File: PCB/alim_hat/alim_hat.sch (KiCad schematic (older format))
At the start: 42 parts, among them J1 Screw_Terminal_01x04, J10 Conn_01x02, J11 Conn_01x02, J12 Conn_01x02, J2 XT30, J3 Conn_02x04_Odd_Even, J4 Jack-DC, J5 Jack-DC, J6 Jack-DC, J7 Jack-DC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

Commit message: complet new polarity protection
update fab file
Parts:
- added D1: MM1Z15, Diode_SMD:D_SOD-123, symbol Device:D_Zener
- added R14: 470k, Resistor_SMD:R_0805_2012Metric, symbol Device:R
- R13: LCSC (none) -> C17513
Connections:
- net GND: now also D1.2 (A), R14.2
- net at Q1.1 (G), R13.2: now also D1.1 (K), R14.1
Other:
- moved on the sheet: Q1, R13
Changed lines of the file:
@@
 L Transistor_FET:IRF540N Q1
 U 1 1 5F94BD9C
-P 7350 2650
-F 0 "Q1" V 7599 2650 50  0000 C CNN
-F 1 "IRFS7530TRLPBF" V 7690 2650 50  0000 C CNN
-F 2 "Package_TO_SOT_SMD:TO-263-2" H 7600 2575 50  0001 L CIN
-F 3 "http://www.irf.com/product-info/datasheets/data/irf540n.pdf" H 7350 2650 50  0001 L CNN
-F 4 "C500544" V 7350 2650 50  0001 C CNN "LCSC"
-	1    7350 2650
-	0    1    1    0
+P 7300 2750
+F 0 "Q1" V 7549 2750 50  0000 C CNN
+F 1 "IRFS7530TRLPBF" V 7640 2750 50  0000 C CNN
+F 2 "Package_TO_SOT_SMD:TO-263-2" H 7550 2675 50  0001 L CIN
+F 3 "http://www.irf.com/product-info/datasheets/data/irf540n.pdf" H 7300 2750 50  0001 L CNN
+F 4 "C500544" V 7300 2750 50  0001 C CNN "LCSC"
+	1    7300 2750
+	0    -1   1    0
 $EndComp
 $Comp
@@
 L power:+12V #PWR0101
 U 1 1 5F9723E9
-P 7350 2150
-F 0 "#PWR0101" H 7350 2000 50  0001 C CNN
-F 1 "+12V" V 7365 2278 50  0000 L CNN
-F 2 "" H 7350 2150 50  0001 C CNN
-F 3 "" H 7350 2150 50  0001 C CNN
-	1    7350 2150
+P 7300 2250
+F 0 "#PWR0101" H 7300 2100 50  0001 C CNN
+F 1 "+12V" V 7315 2378 50  0000 L CNN
+F 2 "" H 7300 2250 50  0001 C CNN
+F 3 "" H 7300 2250 50  0001 C CNN
+	1    7300 2250
 	1    0    0    -1
 $EndComp
@@
 L Device:R R13
 U 1 1 5F972BB9
-P 7350 2300
-F 0 "R13" H 7420 2346 50  0000 L CNN
-F 1 "1k" V 7350 2250 50  0000 L CNN
-F 2 "Resistor_SMD:R_0805_2012Metric" V 7280 2300 50  0001 C CNN
-F 3 "~" H 7350 2300 50  0001 C CNN
-	1    7350 2300
+P 7300 2400
+F 0 "R13" H 7370 2446 50  0000 L CNN
+F 1 "1k" V 7300 2350 50  0000 L CNN
+F 2 "Resistor_SMD:R_0805_2012Metric" V 7230 2400 50  0001 C CNN
+F 3 "~" H 7300 2400 50  0001 C CNN
+F 4 "C17513" H 7300 2400 50  0001 C CNN "LCSC"
+	1    7300 2400
 	1    0    0    -1
 $EndComp
@@
 	-1   0    0    1
 $EndComp
-Text Label 7550 2750 0    50   ~ 0
+Text Label 7100 2850 2    50   ~ 0
 gnd_no
 $Comp
 L power:GND #PWR0105
 U 1 1 5F9B3CAE
-P 7150 2750
-F 0 "#PWR0105" H 7150 2500 50  0001 C CNN
-F 1 "GND" V 7155 2622 50  0000 R CNN
-F 2 "" H 7150 2750 50  0001 C CNN
-F 3 "" H 7150 2750 50  0001 C CNN
-	1    7150 2750
-	0    1    1    0
+P 7850 2850
+F 0 "#PWR0105" H 7850 2600 50  0001 C CNN
+F 1 "GND" V 7855 2722 50  0000 R CNN
+F 2 "" H 7850 2850 50  0001 C CNN
+F 3 "" H 7850 2850 50  0001 C CNN
+	1    7850 2850
+	0    -1   -1   0
 $EndComp
 Text Label 9400 4250 2    50   ~ 0
 gnd_no
 Wire Notes Line
-	6650 1600 8100 1600
-Wire Notes Line
-	8100 1600 8100 3250
-Wire Notes Line
-	8100 3250 6650 3250
+	8300 1600 8300 3250
 Wire Notes Line
 	6650 3250 6650 1600
@@
 	-1   0    0    -1
 $EndComp
+$Comp
+L Device:R R14
+U 1 1 5F99B8E4
+P 7600 2700
+F 0 "R14" H 7670 2746 50  0000 L CNN
+F 1 "470k" V 7600 2600 50  0000 L CNN
+F 2 "Resistor_SMD:R_0805_2012Metric" V 7530 2700 50  0001 C CNN
+F 3 "~" H 7600 2700 50  0001 C CNN
+F 4 "C17709" H 7600 2700 50  0001 C CNN "LCSC"
+	1    7600 2700
+	1    0    0    -1
+$EndComp
+$Comp
+L Device:D_Zener D1
+U 1 1 5F9A9262
+P 7850 2700
+F 0 "D1" V 7804 2779 50  0000 L CNN
+F 1 "MM1Z15" V 7895 2779 50  0000 L CNN
+F 2 "Diode_SMD:D_SOD-123" H 7850 2700 50  0001 C CNN
+F 3 "~" H 7850 2700 50  0001 C CNN
+F 4 "C86235" V 7850 2700 50  0001 C CNN "LCSC"
+	1    7850 2700
+	0    1    1    0
+$EndComp
+Wire Wire Line
+	7500 2850 7600 2850
+Connection ~ 7600 2850
+Wire Wire Line
+	7600 2850 7850 2850
+Connection ~ 7850 2850
+Wire Wire Line
+	7850 2550 7600 2550
+Connection ~ 7600 2550
+Wire Wire Line
+	7300 2550 7600 2550
+Connection ~ 7300 2550
+Wire Notes Line
+	6650 1600 8300 1600
+Wire Notes Line
+	6650 3250 8300 3250
 $EndSCHEMATC

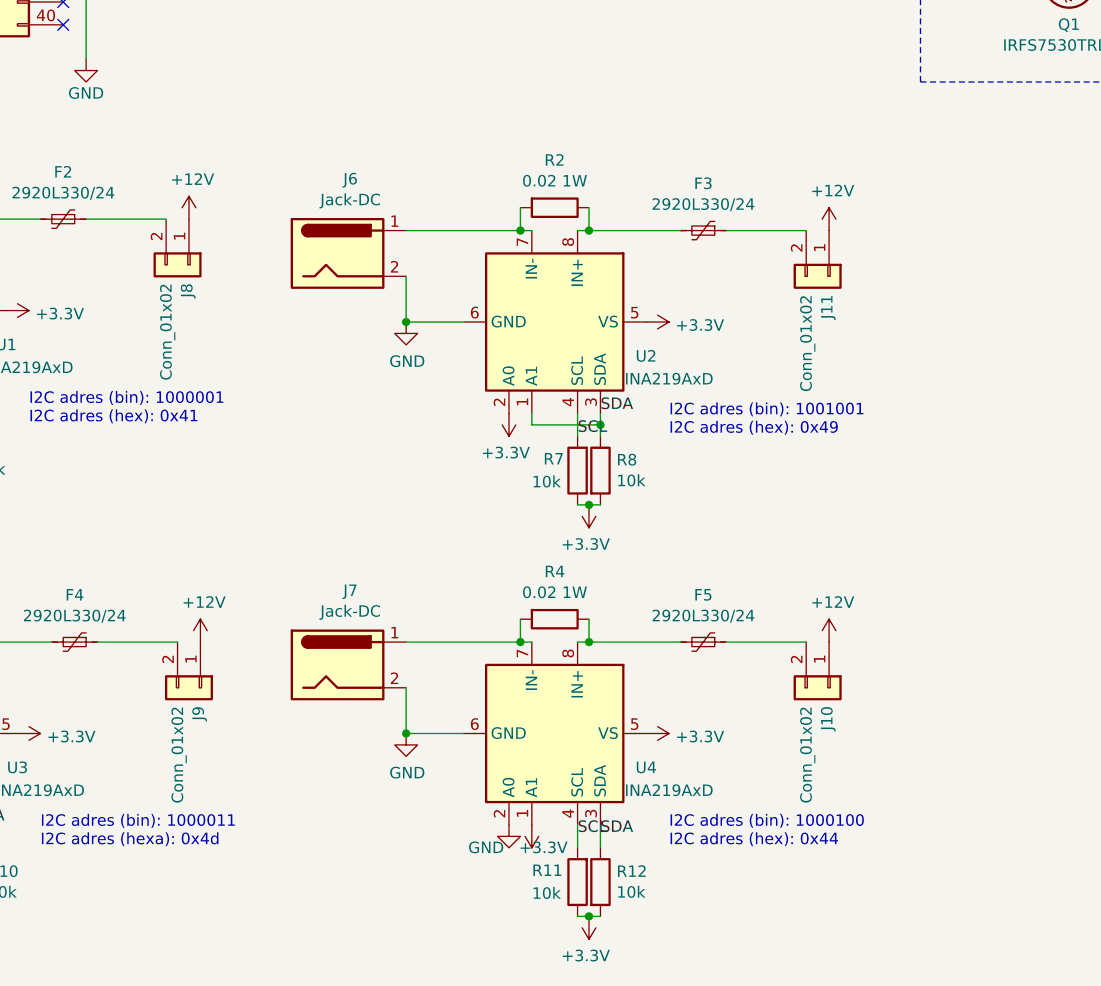
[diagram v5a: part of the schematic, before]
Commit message: update alim and relais pcb 2-> 4 couches
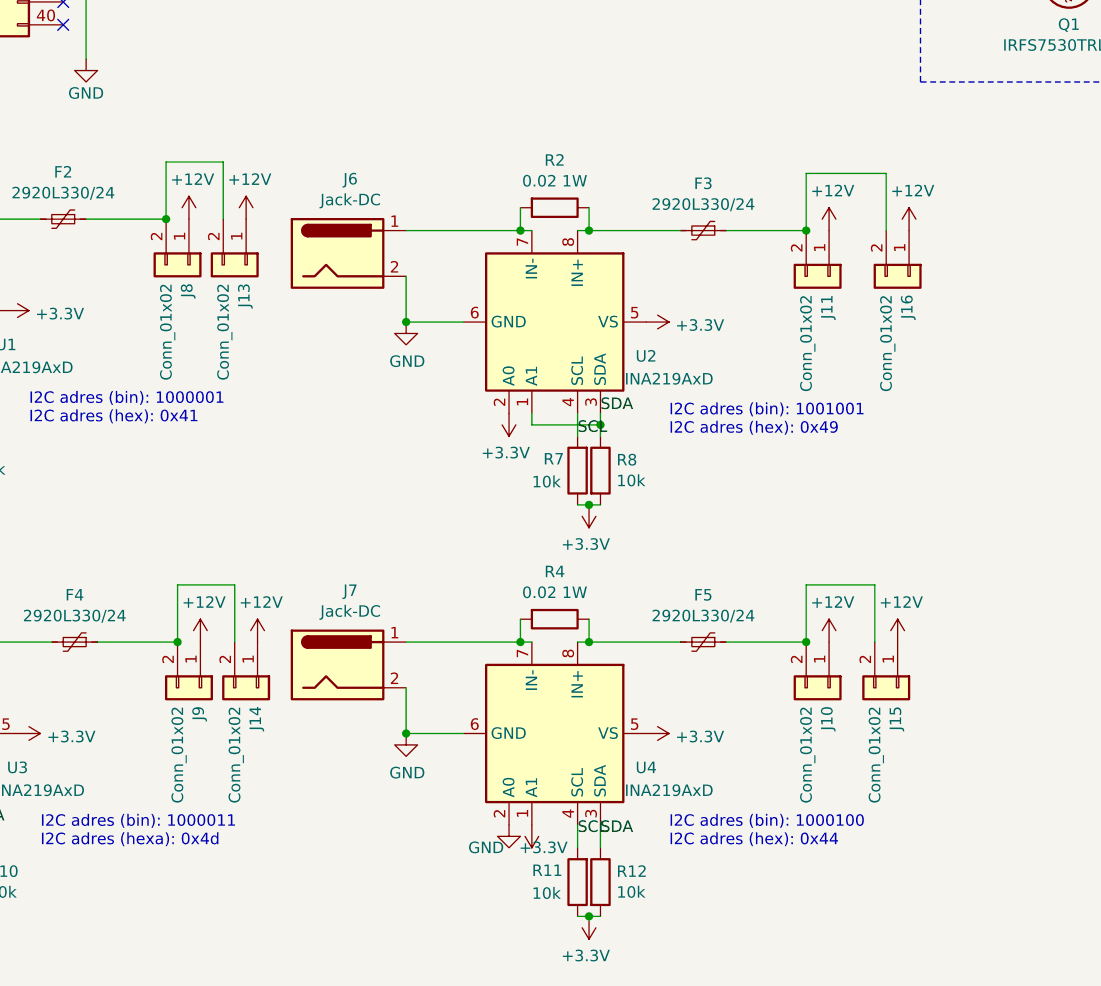
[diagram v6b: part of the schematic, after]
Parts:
- added J13, J14, J15, J16: Conn_01x02, Connector_PinHeader_2.54mm:PinHeader_1x02_P2.54mm_Vertical, symbol Connector_Generic:Conn_01x02
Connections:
- net +12V: now also J13.1 (Pin_1), J14.1 (Pin_1), J15.1 (Pin_1), J16.1 (Pin_1)
- net at F4.1, J9.2 (Pin_2): now also J14.2 (Pin_2)
- net at F2.1, J8.2 (Pin_2): now also J13.2 (Pin_2)
- net at F5.1, J10.2 (Pin_2): now also J15.2 (Pin_2)
- net at F3.1, J11.2 (Pin_2): now also J16.2 (Pin_2)
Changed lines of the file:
@@
 Wire Notes Line
 	6650 3250 8300 3250
+$Comp
+L Connector_Generic:Conn_01x02 J?
+U 1 1 5F9A4F89
+P 6600 4100
+AR Path="/5E5C0CC9/5F9A4F89" Ref="J?"  Part="1"
+AR Path="/5F9A4F89" Ref="J16"  Part="1"
+F 0 "J16" H 6680 4092 50  0000 L CNN
+F 1 "Conn_01x02" H 6680 4001 50  0000 L CNN
+F 2 "Connector_PinHeader_2.54mm:PinHeader_1x02_P2.54mm_Vertical" H 6600 4100 50  0001 C CNN
+F 3 "~" H 6600 4100 50  0001 C CNN
+	1    6600 4100
+	0    1    1    0
+$EndComp
+$Comp
+L Connector_Generic:Conn_01x02 J?
+U 1 1 5F9A9224
+P 6550 5900
+AR Path="/5E5C0CC9/5F9A9224" Ref="J?"  Part="1"
+AR Path="/5F9A9224" Ref="J15"  Part="1"
+F 0 "J15" H 6630 5892 50  0000 L CNN
+F 1 "Conn_01x02" H 6630 5801 50  0000 L CNN
+F 2 "Connector_PinHeader_2.54mm:PinHeader_1x02_P2.54mm_Vertical" H 6550 5900 50  0001 C CNN
+F 3 "~" H 6550 5900 50  0001 C CNN
+	1    6550 5900
+	0    1    1    0
+$EndComp
+$Comp
+L Connector_Generic:Conn_01x02 J?
+U 1 1 5F9ADCF2
+P 3750 5900
+AR Path="/5E5C0CC9/5F9ADCF2" Ref="J?"  Part="1"
+AR Path="/5F9ADCF2" Ref="J14"  Part="1"
+F 0 "J14" H 3830 5892 50  0000 L CNN
+F 1 "Conn_01x02" H 3830 5801 50  0000 L CNN
+F 2 "Connector_PinHeader_2.54mm:PinHeader_1x02_P2.54mm_Vertical" H 3750 5900 50  0001 C CNN
+F 3 "~" H 3750 5900 50  0001 C CNN
+	1    3750 5900
+	0    1    1    0
+$EndComp
+$Comp
+L Connector_Generic:Conn_01x02 J?
+U 1 1 5F9B1FB3
+P 3700 4050
+AR Path="/5E5C0CC9/5F9B1FB3" Ref="J?"  Part="1"
+AR Path="/5F9B1FB3" Ref="J13"  Part="1"
+F 0 "J13" H 3780 4042 50  0000 L CNN
+F 1 "Conn_01x02" H 3780 3951 50  0000 L CNN
+F 2 "Connector_PinHeader_2.54mm:PinHeader_1x02_P2.54mm_Vertical" H 3700 4050 50  0001 C CNN
+F 3 "~" H 3700 4050 50  0001 C CNN
+	1    3700 4050
+	0    1    1    0
+$EndComp
+Wire Wire Line
+	3350 3850 3350 3600
+Wire Wire Line
+	3350 3600 3600 3600
+Wire Wire Line
+	3600 3600 3600 3850
+Connection ~ 3350 3850
+Wire Wire Line
+	6150 3900 6150 3650
+Wire Wire Line
+	6150 3650 6500 3650
+Wire Wire Line
+	6500 3650 6500 3900
+Connection ~ 6150 3900
+Wire Wire Line
+	6150 5700 6150 5450
+Wire Wire Line
+	6150 5450 6450 5450
+Wire Wire Line
+	6450 5450 6450 5700
+Connection ~ 6150 5700
+Wire Wire Line
+	3400 5700 3400 5450
+Wire Wire Line
+	3400 5450 3650 5450
+Wire Wire Line
+	3650 5450 3650 5700
+Connection ~ 3400 5700
+$Comp
+L power:+12V #PWR0110
+U 1 1 5F9CEDA4
+P 3750 5700
+F 0 "#PWR0110" H 3750 5550 50  0001 C CNN
+F 1 "+12V" H 3765 5873 50  0000 C CNN
+F 2 "" H 3750 5700 50  0001 C CNN
+F 3 "" H 3750 5700 50  0001 C CNN
+	1    3750 5700
+	1    0    0    -1
+$EndComp
+$Comp
+L power:+12V #PWR0141
+U 1 1 5F9CFB9A
+P 6550 5700
+F 0 "#PWR0141" H 6550 5550 50  0001 C CNN
+F 1 "+12V" H 6565 5873 50  0000 C CNN
+F 2 "" H 6550 5700 50  0001 C CNN
+F 3 "" H 6550 5700 50  0001 C CNN
+	1    6550 5700
+	1    0    0    -1
+$EndComp
+$Comp
+L power:+12V #PWR0142
+U 1 1 5F9D054A
+P 6600 3900
+F 0 "#PWR0142" H 6600 3750 50  0001 C CNN
+F 1 "+12V" H 6615 4073 50  0000 C CNN
+F 2 "" H 6600 3900 50  0001 C CNN
+F 3 "" H 6600 3900 50  0001 C CNN
+	1    6600 3900
+	1    0    0    -1
+$EndComp
+$Comp
+L power:+12V #PWR0143
+U 1 1 5F9D0F11
+P 3700 3850
+F 0 "#PWR0143" H 3700 3700 50  0001 C CNN
+F 1 "+12V" H 3715 4023 50  0000 C CNN
+F 2 "" H 3700 3850 50  0001 C CNN
+F 3 "" H 3700 3850 50  0001 C CNN
+	1    3700 3850
+	1    0    0    -1
+$EndComp
 $EndSCHEMATC

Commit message: ajust all board
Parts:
- C1, C2: value 100uF -> 100uF 35V; LCSC C311622 -> C134792
- F2, F3, F4: value 2920L330/24 -> SMD1812P300SLR/24; footprint fuse:THRMC7451X160N -> Fuse:Fuse_1812_4532Metric; LCSC (none) -> C495359
- F5: value 2920L330/24 -> SMD1812P300SLR/24; footprint fuse:THRMC7451X160N -> Fuse:Fuse_1812_4532Metric; LCSC (none) -> SMD1812P300SLR/24
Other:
- note added: "or\n1812L300/24SL"
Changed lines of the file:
@@
 Sheet 1 1
 Title ""
-Date "15 nov 2012"
-Rev ""
+Date "2020-10-30"
+Rev "4.0"
 Comp ""
 Comment1 ""
@@
 P 8100 5550
 F 0 "C1" H 8218 5596 50  0000 L CNN
-F 1 "100uF" H 8218 5505 50  0000 L CNN
+F 1 "100uF 35V" H 8218 5505 50  0000 L CNN
 F 2 "capa:CAPAE660X800N" H 8138 5400 50  0001 C CNN
 F 3 "~" H 8100 5550 50  0001 C CNN
-F 4 "C311622" H 8100 5550 50  0001 C CNN "LCSC"
+F 4 "C134792" H 8100 5550 50  0001 C CNN "LCSC"
 	1    8100 5550
 	1    0    0    -1
@@
 P 10550 5550
 F 0 "C2" H 10668 5596 50  0000 L CNN
-F 1 "100uF" H 10668 5505 50  0000 L CNN
+F 1 "100uF 35V" H 10668 5505 50  0000 L CNN
 F 2 "capa:CAPAE660X800N" H 10588 5400 50  0001 C CNN
 F 3 "~" H 10550 5550 50  0001 C CNN
-F 4 "C311622" H 10550 5550 50  0001 C CNN "LCSC"
+F 4 "C134792" H 10550 5550 50  0001 C CNN "LCSC"
 	1    10550 5550
 	1    0    0    -1
@@
 AR Path="/5E5E1105" Ref="F4"  Part="1"
 F 0 "F4" V 2745 5700 50  0000 C CNN
-F 1 "2920L330/24" V 2836 5700 50  0000 C CNN
-F 2 "fuse:THRMC7451X160N" H 3000 5500 50  0001 L CNN
+F 1 "SMD1812P300SLR/24" V 2836 5700 50  0000 C CNN
+F 2 "Fuse:Fuse_1812_4532Metric" H 3000 5500 50  0001 L CNN
 F 3 "~" H 2950 5700 50  0001 C CNN
-F 4 "" V 2950 5700 50  0001 C CNN "LCSC"
+F 4 "C495359" V 2950 5700 50  0001 C CNN "LCSC"
 	1    2950 5700
 	0    1    1    0
@@
 $EndComp
 $Comp
-L Device:Polyfuse_Small F?
-U 1 1 5E5E115F
-P 2900 3850
-AR Path="/5E5C0CC9/5E5E115F" Ref="F?"  Part="1"
-AR Path="/5E5E115F" Ref="F2"  Part="1"
-F 0 "F2" V 2695 3850 50  0000 C CNN
-F 1 "2920L330/24" V 2786 3850 50  0000 C CNN
-F 2 "fuse:THRMC7451X160N" H 2950 3650 50  0001 L CNN
-F 3 "~" H 2900 3850 50  0001 C CNN
-F 4 "" V 2900 3850 50  0001 C CNN "LCSC"
-	1    2900 3850
-	0    1    1    0
-$EndComp
-$Comp
 L power:+12V #PWR?
 U 1 1 5E5E116B
@@
 $EndComp
 $Comp
-L Device:Polyfuse_Small F?
-U 1 1 5E5E11BF
-P 5700 5700
-AR Path="/5E5C0CC9/5E5E11BF" Ref="F?"  Part="1"
-AR Path="/5E5E11BF" Ref="F5"  Part="1"
-F 0 "F5" V 5495 5700 50  0000 C CNN
-F 1 "2920L330/24" V 5586 5700 50  0000 C CNN
-F 2 "fuse:THRMC7451X160N" H 5750 5500 50  0001 L CNN
-F 3 "~" H 5700 5700 50  0001 C CNN
-F 4 "" V 5700 5700 50  0001 C CNN "LCSC"
-	1    5700 5700
-	0    1    1    0
-$EndComp
-$Comp
 L Analog_ADC:INA219AxD U?
 U 1 1 5E5E11C5
@@
 AR Path="/5E5E121F" Ref="F3"  Part="1"
 F 0 "F3" V 5495 3900 50  0000 C CNN
-F 1 "2920L330/24" V 5586 3900 50  0000 C CNN
-F 2 "fuse:THRMC7451X160N" H 5750 3700 50  0001 L CNN
+F 1 "SMD1812P300SLR/24" V 5586 3900 50  0000 C CNN
+F 2 "Fuse:Fuse_1812_4532Metric" H 5750 3700 50  0001 L CNN
 F 3 "~" H 5700 3900 50  0001 C CNN
-F 4 "" V 5700 3900 50  0001 C CNN "LCSC"
+F 4 "C495359" V 5700 3900 50  0001 C CNN "LCSC"
 	1    5700 3900
 	0    1    1    0
@@
 	1    0    0    -1
 $EndComp
+$Comp
+L Device:Polyfuse_Small F?
+U 1 1 5E5E11BF
+P 5700 5700
+AR Path="/5E5C0CC9/5E5E11BF" Ref="F?"  Part="1"
+AR Path="/5E5E11BF" Ref="F5"  Part="1"
+F 0 "F5" V 5495 5700 50  0000 C CNN
+F 1 "SMD1812P300SLR/24" V 5600 5700 50  0000 C CNN
+F 2 "Fuse:Fuse_1812_4532Metric" H 5750 5500 50  0001 L CNN
+F 3 "~" H 5700 5700 50  0001 C CNN
+F 4 "SMD1812P300SLR/24" V 5700 5700 50  0001 C CNN "LCSC"
+	1    5700 5700
+	0    1    1    0
+$EndComp
+$Comp
+L Device:Polyfuse_Small F?
+U 1 1 5E5E115F
+P 2900 3850
+AR Path="/5E5C0CC9/5E5E115F" Ref="F?"  Part="1"
+AR Path="/5E5E115F" Ref="F2"  Part="1"
+F 0 "F2" V 2695 3850 50  0000 C CNN
+F 1 "SMD1812P300SLR/24" V 2786 3850 50  0000 C CNN
+F 2 "Fuse:Fuse_1812_4532Metric" H 2950 3650 50  0001 L CNN
+F 3 "~" H 2900 3850 50  0001 C CNN
+F 4 "C495359" V 2900 3850 50  0001 C CNN "LCSC"
+	1    2900 3850
+	0    1    1    0
+$EndComp
+Text Notes 5400 5900 0    50   ~ 0
+or\n1812L300/24SL
+Text Notes 5450 4100 0    50   ~ 0
+or\n1812L300/24SL
+Text Notes 2650 4050 0    50   ~ 0
+or\n1812L300/24SL
+Text Notes 2650 5900 0    50   ~ 0
+or\n1812L300/24SL
 $EndSCHEMATC

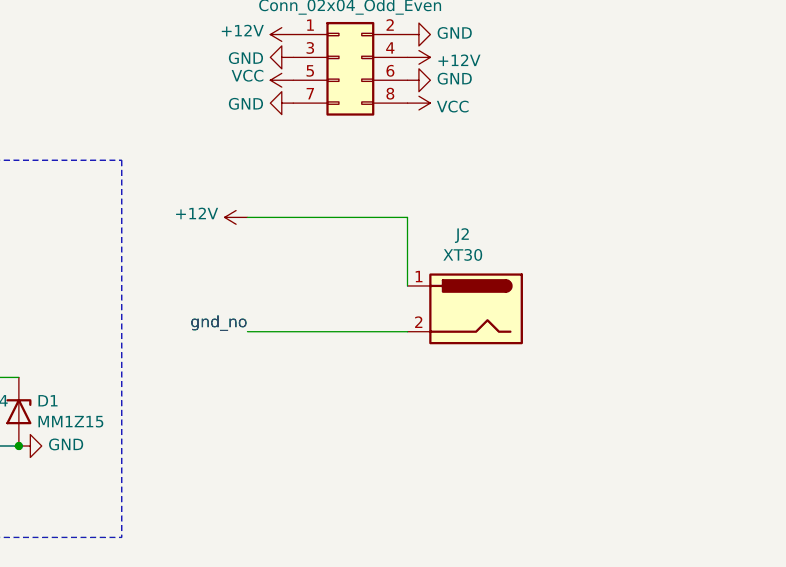
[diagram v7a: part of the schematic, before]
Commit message: invert polarity xt30 connector
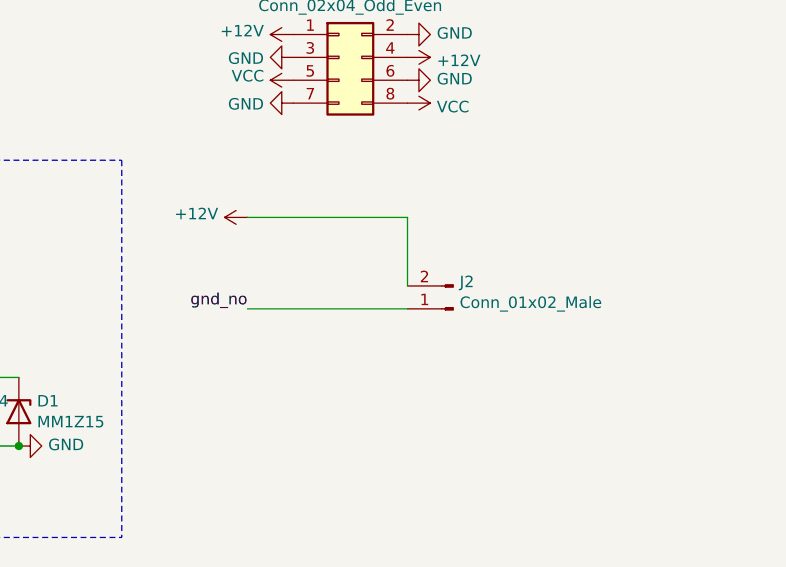
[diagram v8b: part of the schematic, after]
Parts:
- removed J2: XT30, Connector_AMASS:AMASS_XT30PW-M_1x02_P2.50mm_Horizontal, symbol Connector:Jack-DC
- added J2: Conn_01x02_Male, Connector_AMASS:AMASS_XT30PW-M_1x02_P2.50mm_Horizontal, symbol Connector:Conn_01x02_Male
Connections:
- net +12V: now also J2.2 (Pin_2)
- net gnd_no: now also J2.1 (Pin_1)
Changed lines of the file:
@@
 Sheet 1 1
 Title ""
-Date "2020-10-30"
-Rev "4.0"
+Date "2020-11-18"
+Rev "4.1"
 Comp ""
 Comment1 ""
@@
 $EndComp
 Wire Wire Line
-	8850 2350 9550 2350
+	8850 2250 9550 2250
 Wire Wire Line
 	8850 1850 9550 1850
@@
 	1    0    0    -1
 $EndComp
-Text Label 8850 2350 2    50   ~ 0
+Text Label 8850 2250 2    50   ~ 0
 gnd_no
 $Comp
@@
 Text Notes 6700 1700 0    50   ~ 0
 Polarity protection
-$Comp
-L Connector:Jack-DC J?
-U 1 1 5F50DE31
-P 9850 2250
-AR Path="/5E5C0CC9/5F50DE31" Ref="J?"  Part="1"
-AR Path="/5F50DE31" Ref="J2"  Part="1"
-F 0 "J2" H 9907 2575 50  0000 C CNN
-F 1 "XT30" H 9907 2484 50  0000 C CNN
-F 2 "Connector_AMASS:AMASS_XT30PW-M_1x02_P2.50mm_Horizontal" H 9900 2210 50  0001 C CNN
-F 3 "~" H 9900 2210 50  0001 C CNN
-	1    9850 2250
-	-1   0    0    -1
-$EndComp
 $Comp
 L Device:R R14
@@
 Text Notes 2650 5900 0    50   ~ 0
 or\n1812L300/24SL
+$Comp
+L Connector:Conn_01x02_Male J2
+U 1 1 5FB61870
+P 9750 2250
+F 0 "J2" H 9722 2132 50  0000 R CNN
+F 1 "Conn_01x02_Male" H 9722 2223 50  0000 R CNN
+F 2 "Connector_AMASS:AMASS_XT30PW-M_1x02_P2.50mm_Horizontal" H 9750 2250 50  0001 C CNN
+F 3 "~" H 9750 2250 50  0001 C CNN
+	1    9750 2250
+	-1   0    0    1
+$EndComp
 $EndSCHEMATC
